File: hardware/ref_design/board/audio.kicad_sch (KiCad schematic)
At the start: 15 parts, among them J4 SPEAKER, Q3 2N7002, U7 FM8002A

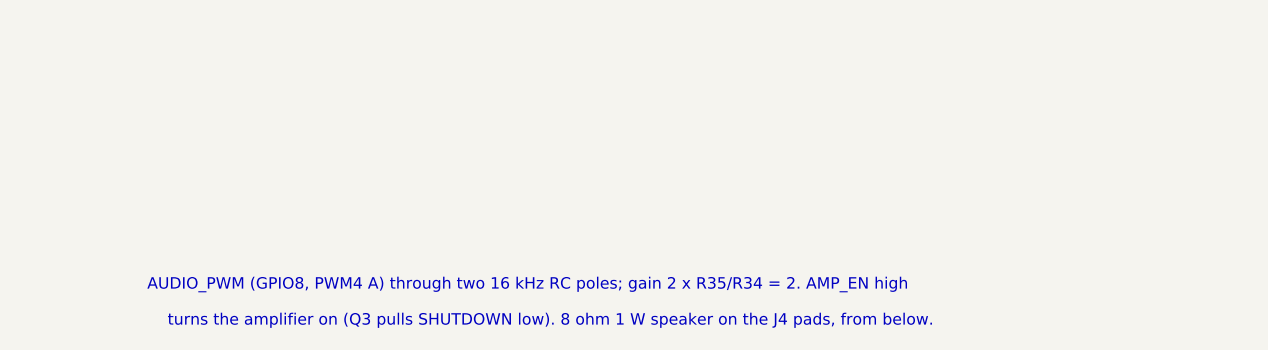
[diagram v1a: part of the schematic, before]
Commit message: Reference design: docs from the model review panel (audio, off-state, unplug)
A panel of seven other model families reviewed the board through pi; Fable
verified their eight distinct claims against the datasheets. None changes the
hardware; the confirmed ones correct the docs:
- Audio: the two RC stages give -3 dB at about 6.6 kHz loaded (not two
  16 kHz poles); full scale is about 0.55 W on USB and 0.4-0.5 W on the cell
  (not 1 W); the FM8002A takes about 100 ms to wake, so AMP_EN stays on while
  awake or rises well ahead of a sound. Bring-up step 4 now measures that
  delay and checks U7's temperature at full scale on USB.
- Off state: with the chip unpowered GPIO47 sits above IOVDD, clamped by its
  ESD diode at under 9 uA: accepted, and the off-state budget is 12-16 uA.
- design.py's load-sharing comment no longer claims a microsecond hand-over.
- The rules note says the membrane contacts leave on 0.2 mm stubs.
Rejected: RUN needs an external pull-up (it has an internal one), VSYS
routed at 0.2 mm (only the power button's contact stub).

Checks: netlist PASS, ERC 0, DRC 0 errors / 0 unconnected / 0 parity.

Co-Authored-By: Claude Opus 5.5 <noreply@anthropic.com>
Claude-Session: https://claude.ai/code/session_01KGgEu3CbFtCsvHRQgAFiCN
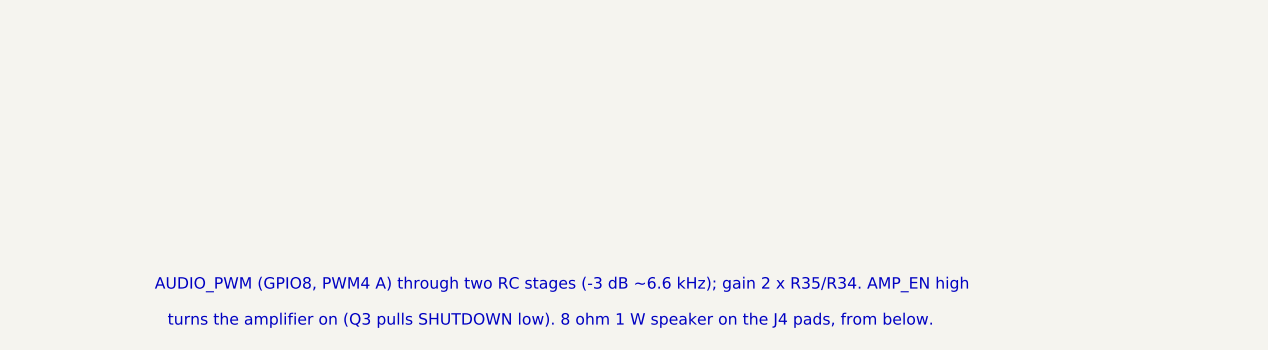
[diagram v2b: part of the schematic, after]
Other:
- note added: "AUDIO_PWM (GPIO8, PWM4 A) through two RC stages (-3 dB ~6.6 kHz); gain 2 x R35/R34. AMP_EN high"
- note removed: "AUDIO_PWM (GPIO8, PWM4 A) through two 16 kHz RC poles; gain 2 x R35/R34 = 2. AMP_EN high"
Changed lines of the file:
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@@
       (xy 266.7 38.1))
 )
-  (text "AUDIO_PWM (GPIO8, PWM4 A) through two 16 kHz RC poles; gain 2 x R35/R34 = 2. AMP_EN high"
-    (at 58.42 160 0)
+  (text "AUDIO_PWM (GPIO8, PWM4 A) through two RC stages (-3 dB ~6.6 kHz); gain 2 x R35/R34. AMP_EN high"
+    (at 62.23 160 0)
     (effects
       (font

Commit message: Reference design: audio filter 4.7 nF, PWM at 8 bits (586 kHz)
C37/C38 10 nF -> 4.7 nF (C1538, a JLC basic part; C37/C38 were the only
users of the 10 nF part, so the BOM stays at 37 part numbers). With the PWM
at 8 bits (150 MHz / 256 = 586 kHz) the audio band is -3 dB at about 14 kHz
instead of 6.6 kHz, and the carrier comes out 49 dB down instead of 38.
Firmware must run 8 bits: 10-bit PWM (146 kHz) would only be 26 dB down.
Pin map, bring-up, design review, PLAN and the schematic note say so.
(3.9 nF, which would give 17 kHz, is only an extended part at JLC.)

Checks: netlist PASS, ERC 0, DRC 0 errors / 0 unconnected / 0 parity,
fit PASS.

Co-Authored-By: Claude Opus 5.5 <noreply@anthropic.com>
Claude-Session: https://claude.ai/code/session_01KGgEu3CbFtCsvHRQgAFiCN
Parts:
- C37, C38: value 10n -> 4.7n; LCSC C15195 -> C1538; MPN CL05B103KB5NNNC -> 0402B472K500NT
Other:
- note added: "AUDIO_PWM (GPIO8, PWM4 A, 8 bits: 586 kHz) through two RC stages (-3 dB ~14 kHz); gain 2 x R35/R34. AMP_EN high"
- note removed: "AUDIO_PWM (GPIO8, PWM4 A) through two RC stages (-3 dB ~6.6 kHz); gain 2 x R35/R34. AMP_EN high"
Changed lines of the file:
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@@
       (xy 266.7 38.1))
 )
-  (text "AUDIO_PWM (GPIO8, PWM4 A) through two RC stages (-3 dB ~6.6 kHz); gain 2 x R35/R34. AMP_EN high"
-    (at 62.23 160 0)
+  (text "AUDIO_PWM (GPIO8, PWM4 A, 8 bits: 586 kHz) through two RC stages (-3 dB ~14 kHz); gain 2 x R35/R34. AMP_EN high"
+    (at 69.85 160 0)
     (effects
       (font
@@
         (font
           (size 1.27 1.27))))
-    (property "Value" "10n"
+    (property "Value" "4.7n"
       (at 124.46 31.75 0)
       (effects
@@
           (size 1.27 1.27))
         (hide yes)))
-    (property "LCSC" "C15195"
-      (at 0 0 0)
-      (effects
-        (font
-          (size 1.27 1.27))
-        (hide yes)))
-    (property "MPN" "CL05B103KB5NNNC"
+    (property "LCSC" "C1538"
+      (at 0 0 0)
+      (effects
+        (font
+          (size 1.27 1.27))
+        (hide yes)))
+    (property "MPN" "0402B472K500NT"
       (at 0 0 0)
       (effects
@@
         (font
           (size 1.27 1.27))))
-    (property "Value" "10n"
+    (property "Value" "4.7n"
       (at 195.58 31.75 0)
       (effects
@@
           (size 1.27 1.27))
         (hide yes)))
-    (property "LCSC" "C15195"
-      (at 0 0 0)
-      (effects
-        (font
-          (size 1.27 1.27))
-        (hide yes)))
-    (property "MPN" "CL05B103KB5NNNC"
-      (at 0 0 0)
-      (effects
+    (property "LCSC" "C1538"
+      (at 0 0 0)
+      (effects
+        (font
+          (size 1.27 1.27))
+        (hide yes)))
+    (property "MPN" "0402B472K500NT"
+      (at 0 0 0)
+      (effects

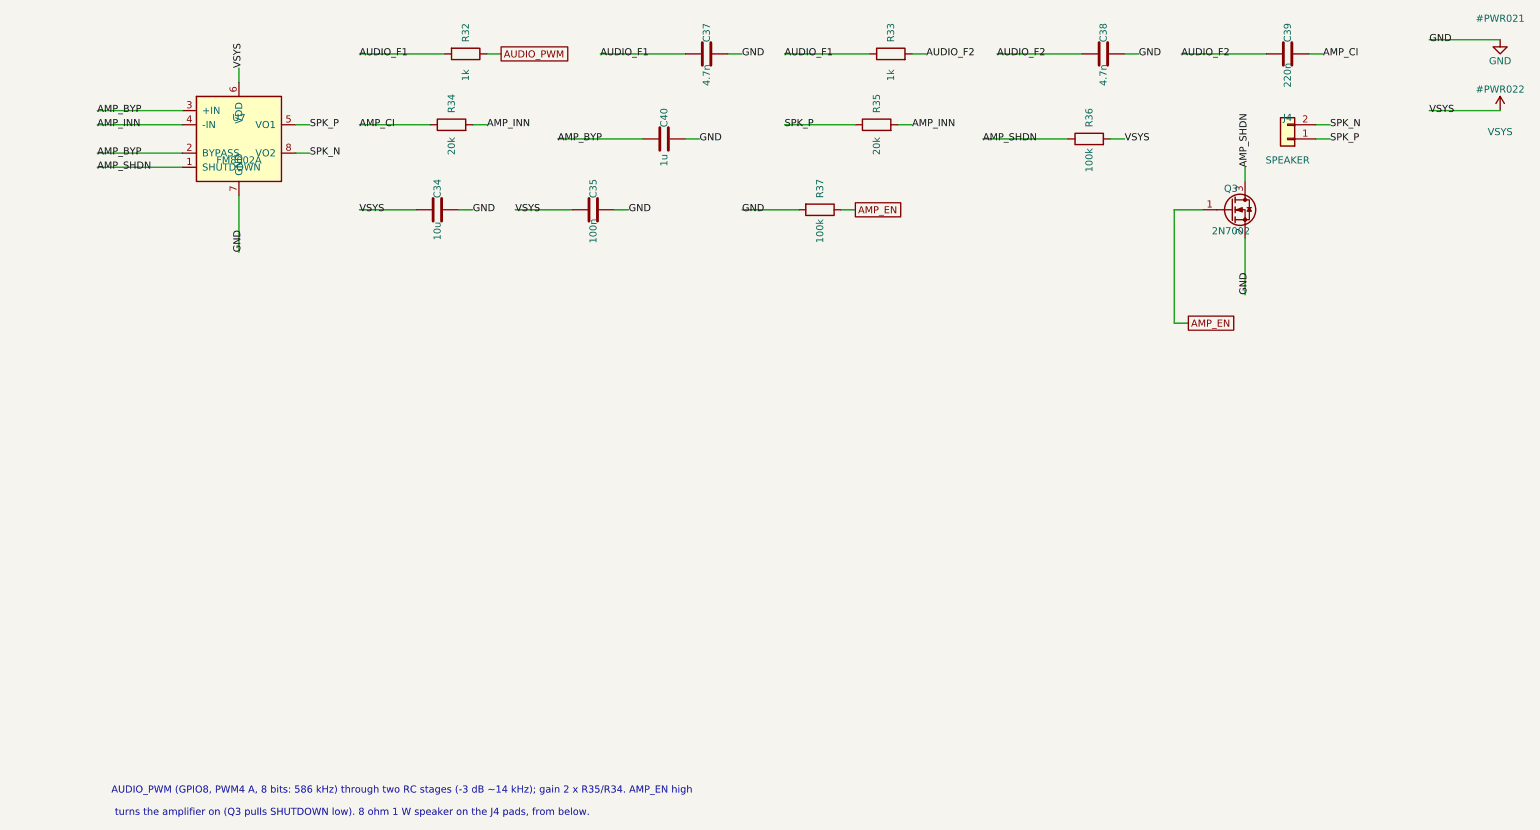
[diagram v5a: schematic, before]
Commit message: Reference design: checklist changes and the datasheet pin gate
Board: PWR_HOLD pull-down (R42, also covers RP2350-E9), charge current
3.3k (333-364 mA), firmware charge pause (CHG_OFF, Q4), R13 33k, 0.1 ohm
in D5's path, JP1/JP2 cut-jumpers, TP6-8, spare 1206 footprints, 4-bit
revision strap on GPIO22-25 (REV 1 on the back).

Datasheet review of every part's pins (pin_review/, tools/check_pins.py)
found and fixed: J6 TX/RX swapped against Raspberry Pi's debug connector
spec, USB series resistors 22 to 27 ohm, the ME6211 CE able to lead its
VIN at a live plug-in (C47 on PWR_EN).

Case: silicone height 1.2 mm from the DS Lite, chamfered step.

Co-Authored-By: Claude Opus 5.5 <noreply@anthropic.com>
Claude-Session: https://claude.ai/code/session_01MUt6paNsT75sqwAr83zRS3
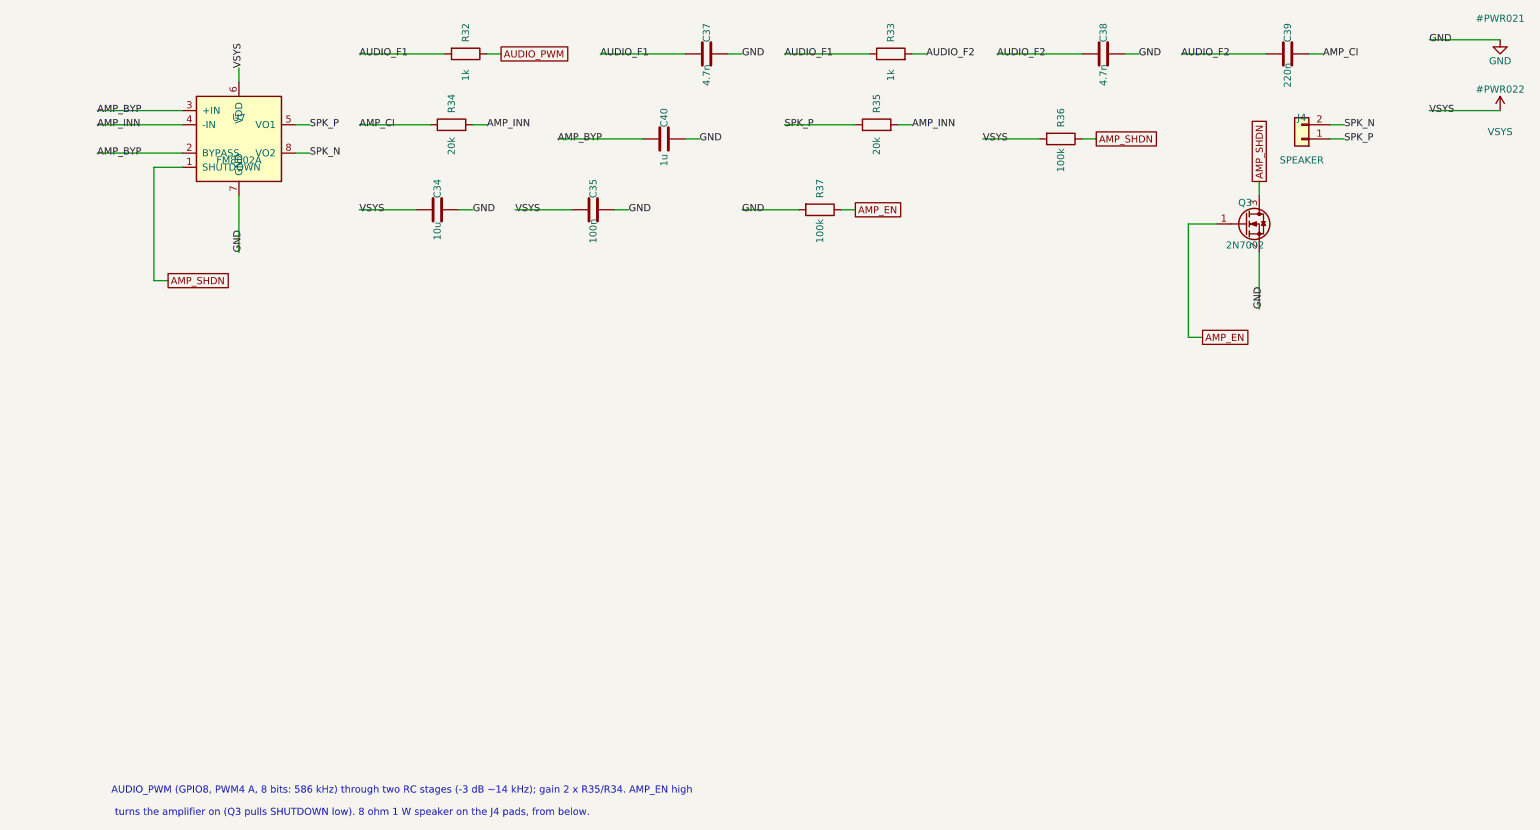
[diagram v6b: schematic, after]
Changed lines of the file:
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@@
-  (wire
-    (pts
-      (xy 30.48 48.26)
-      (xy 15.24 48.26))
-)
   (wire
     (pts
@@
   (wire
     (pts
+      (xy 30.48 48.26)
+      (xy 25.4 48.26))
+)
+  (wire
+    (pts
+      (xy 25.4 48.26)
+      (xy 25.4 68.58))
+)
+  (wire
+    (pts
+      (xy 25.4 68.58)
+      (xy 27.94 68.58))
+)
+  (wire
+    (pts
       (xy 85.09 27.94)
       (xy 87.63 27.94))
@@
   (wire
     (pts
-      (xy 189.23 43.18)
+      (xy 191.77 43.18)
+      (xy 194.31 43.18))
+)
+  (wire
+    (pts
+      (xy 184.15 43.18)
       (xy 173.99 43.18))
 )
   (wire
     (pts
-      (xy 196.85 43.18)
-      (xy 199.39 43.18))
-)
-  (wire
-    (pts
-      (xy 220.98 50.8)
-      (xy 220.98 48.26))
-)
-  (wire
-    (pts
-      (xy 220.98 60.96)
-      (xy 220.98 71.12))
-)
-  (wire
-    (pts
-      (xy 213.36 55.88)
-      (xy 208.28 55.88))
-)
-  (wire
-    (pts
-      (xy 208.28 55.88)
-      (xy 208.28 76.2))
-)
-  (wire
-    (pts
-      (xy 208.28 76.2)
-      (xy 210.82 76.2))
+      (xy 223.52 53.34)
+      (xy 223.52 50.8))
+)
+  (wire
+    (pts
+      (xy 223.52 63.5)
+      (xy 223.52 73.66))
+)
+  (wire
+    (pts
+      (xy 215.9 58.42)
+      (xy 210.82 58.42))
+)
+  (wire
+    (pts
+      (xy 210.82 58.42)
+      (xy 210.82 78.74))
+)
+  (wire
+    (pts
+      (xy 210.82 78.74)
+      (xy 213.36 78.74))
 )
   (wire
@@
   (wire
     (pts
-      (xy 233.68 40.64)
-      (xy 236.22 40.64))
-)
-  (wire
-    (pts
-      (xy 233.68 43.18)
-      (xy 236.22 43.18))
+      (xy 236.22 40.64)
+      (xy 238.76 40.64))
+)
+  (wire
+    (pts
+      (xy 236.22 43.18)
+      (xy 238.76 43.18))
 )
   (wire
@@
     (at 53.34 45.72 0)
 )
-  (label "AMP_SHDN"
-    (at 15.24 48.26 0)
-)
   (label "GND"
     (at 40.64 63.5 90)
@@
     (at 123.19 43.18 0)
 )
-  (label "AMP_SHDN"
+  (label "VSYS"
     (at 173.99 43.18 0)
 )
-  (label "VSYS"
-    (at 199.39 43.18 0)
-)
-  (label "AMP_SHDN"
-    (at 220.98 48.26 90)
-)
   (label "GND"
-    (at 220.98 71.12 90)
+    (at 223.52 73.66 90)
 )
   (label "GND"
@@
 )
   (label "SPK_N"
-    (at 236.22 40.64 0)
+    (at 238.76 40.64 0)
 )
   (label "SPK_P"
-    (at 236.22 43.18 0)
+    (at 238.76 43.18 0)
 )
   (label "GND"
@@
   (label "VSYS"
     (at 254 38.1 0)
+)
+  (global_label "AMP_SHDN"
+    (shape passive)
+    (at 27.94 68.58 0)
 )
   (global_label "AUDIO_PWM"
@@
     (at 87.63 27.94 0)
 )
+  (global_label "AMP_SHDN"
+    (shape passive)
+    (at 194.31 43.18 0)
+)
+  (global_label "AMP_SHDN"
+    (shape passive)
+    (at 223.52 50.8 90)
+)
   (global_label "AMP_EN"
     (shape passive)
-    (at 210.82 76.2 0)
+    (at 213.36 78.74 0)
 )
   (global_label "AMP_EN"
@@
   (symbol
     (lib_id "Device:R")
-    (at 193.04 43.18 90)
+    (at 187.96 43.18 270)
     (unit 1)
     (in_bom yes)
@@
     (dnp no)
     (property "Reference" "R36"
-      (at 193.04 39.37 0)
+      (at 187.96 39.37 0)
       (effects
         (font
           (size 1.27 1.27))))
     (property "Value" "100k"
-      (at 193.04 46.99 0)
+      (at 187.96 46.99 0)
       (effects
         (font
           (size 1.27 1.27))))
     (property "Footprint" "Resistor_SMD:R_0402_1005Metric"
-      (at 193.04 43.18 0)
-      (effects
-        (font
-          (size 1.27 1.27))
-        (hide yes)))
-    (property "Datasheet" ""
-      (at 193.04 43.18 0)
+      (at 187.96 43.18 0)
+      (effects
+        (font
+          (size 1.27 1.27))
+        (hide yes)))
+    (property "Datasheet" ""
+      (at 187.96 43.18 0)
       (effects
         (font
@@
   (symbol
     (lib_id "Transistor_FET:Q_NMOS_GSD")
-    (at 218.44 55.88 0)
+    (at 220.98 58.42 0)
     (unit 1)
     (in_bom yes)
@@
     (dnp no)
     (property "Reference" "Q3"
-      (at 218.44 52.07 0)
+      (at 220.98 54.61 0)
       (effects
         (font
           (size 1.27 1.27))))
     (property "Value" "2N7002"
-      (at 218.44 59.69 0)
+      (at 220.98 62.23 0)
       (effects
         (font
           (size 1.27 1.27))))
     (property "Footprint" "Package_TO_SOT_SMD:SOT-23"
-      (at 218.44 55.88 0)
-      (effects
-        (font
-          (size 1.27 1.27))
-        (hide yes)))
-    (property "Datasheet" ""
-      (at 218.44 55.88 0)
+      (at 220.98 58.42 0)
+      (effects
+        (font
+          (size 1.27 1.27))
+        (hide yes)))
+    (property "Datasheet" ""
+      (at 220.98 58.42 0)
       (effects
         (font
@@
   (symbol
     (lib_id "Connector_Generic:Conn_01x02")
-    (at 228.6 43.18 180)
+    (at 231.14 43.18 180)
     (unit 1)
     (in_bom yes)
@@
     (dnp no)
     (property "Reference" "J4"
-      (at 228.6 39.37 0)
+      (at 231.14 39.37 0)
       (effects
         (font
           (size 1.27 1.27))))
     (property "Value" "SPEAKER"
-      (at 228.6 46.99 0)
+      (at 231.14 46.99 0)
       (effects
         (font
           (size 1.27 1.27))))
     (property "Footprint" "battler:Speaker_Wire_Pads_P4.0mm"
-      (at 228.6 43.18 0)
-      (effects
-        (font
-          (size 1.27 1.27))
-        (hide yes)))
-    (property "Datasheet" ""
-      (at 228.6 43.18 0)
-      (effects
-        (font
+      (at 231.14 43.18 0)
+      (effects
+        (font
+          (size 1.27 1.27))
+        (hide yes)))
+    (property "Datasheet" ""
+      (at 231.14 43.18 0)
+      (effects
+        (font
